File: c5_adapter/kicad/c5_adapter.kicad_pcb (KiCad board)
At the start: 4 copper layers, 50 x 45 mm, 7 parts, among them J1 Conn_01x10, J3 Conn_01x16, J4 Conn_01x16, J5 Conn_01x16, J6 Conn_01x16, SW1 MK-12C02-G020

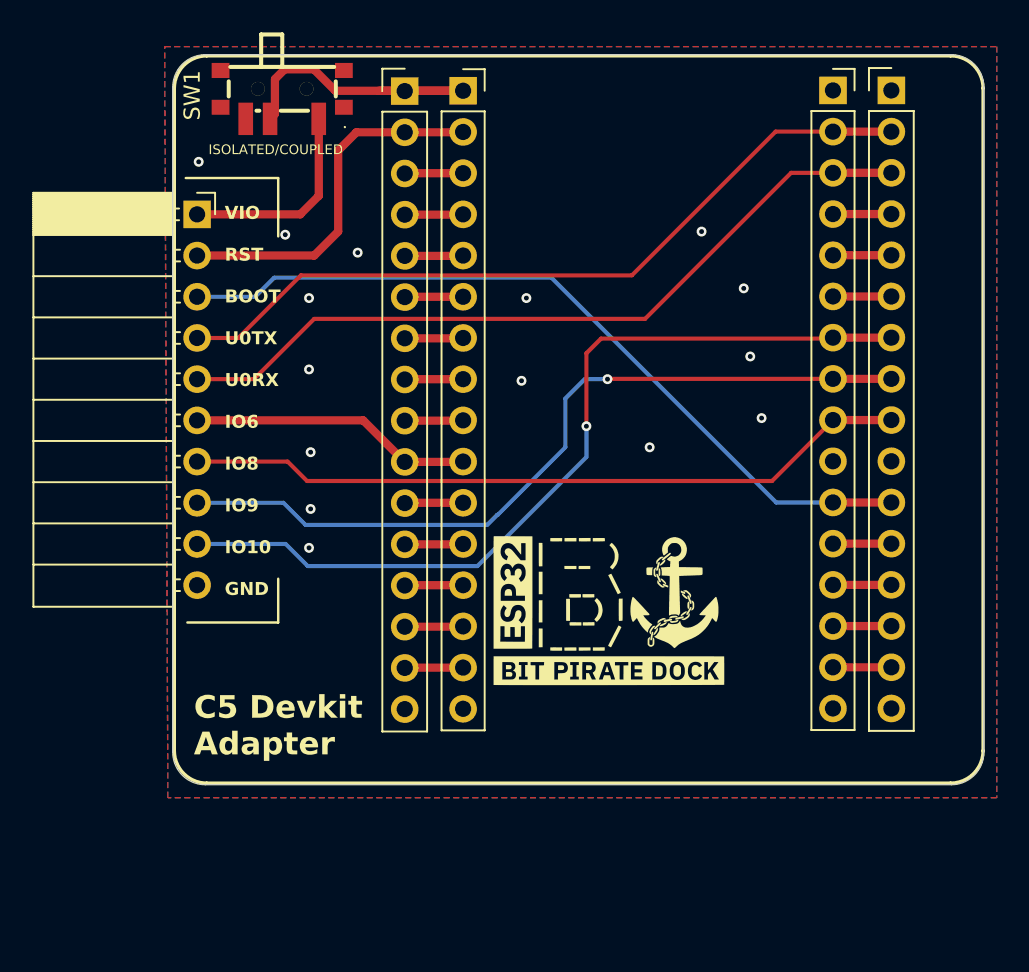
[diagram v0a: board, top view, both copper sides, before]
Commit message: Modified silkscreen markings
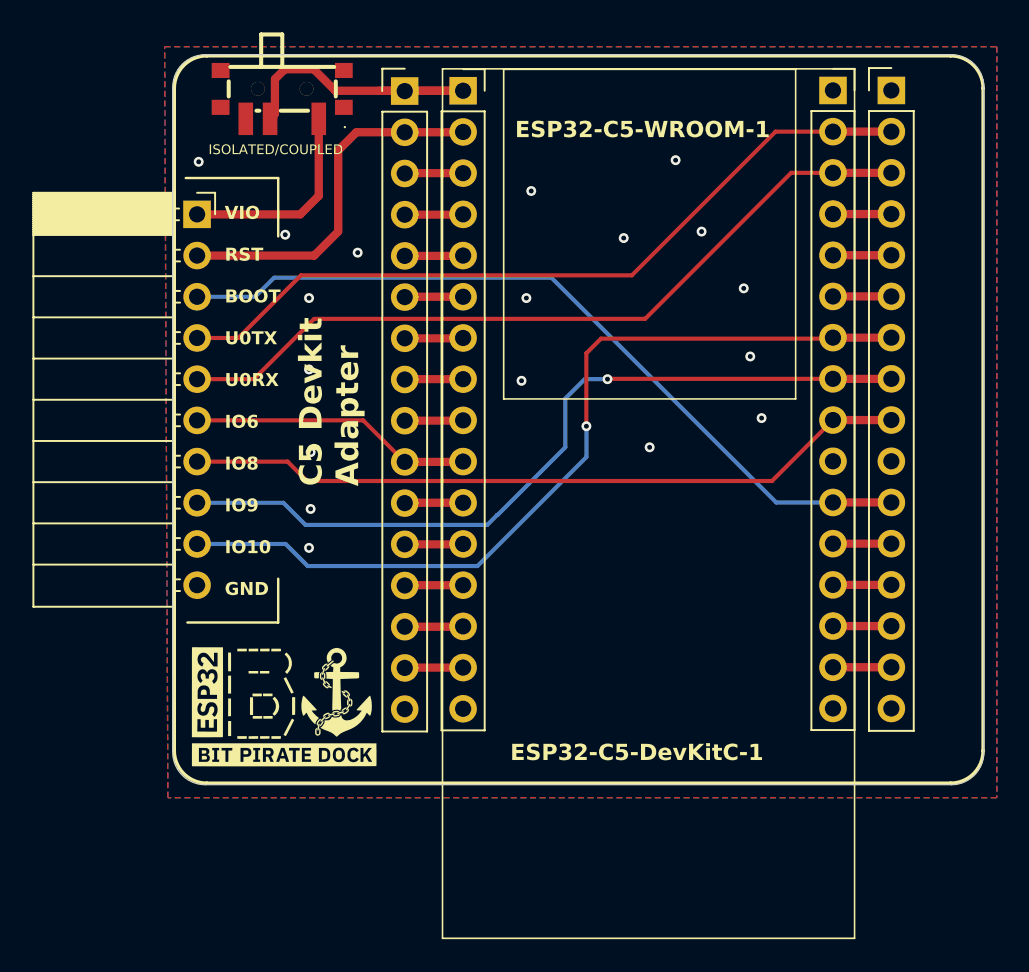
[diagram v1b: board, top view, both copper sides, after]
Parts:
- moved G*** 20.9 mm to (180.0, 118.8)
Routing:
- net GND: vias 15 -> 18
- added copper zone on In1.Cu, net GND
- added copper zone on In2.Cu, net GND
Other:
- board text added: "ESP32-C5-DevKitC-1"
- board text added: "ESP32-C5-WROOM-1"

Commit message: Inverted port writing
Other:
- board text added: "GND IO10 IO9 IO8 IO6 U0RX U0TX BOOT RST VIO"
- board text removed: "VIO RST BOOT U0TX U0RX IO6 IO8 IO9 IO10 GND"
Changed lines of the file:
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@@
 		)
 	)
-	(gr_text "VIO\n\nRST\n\nBOOT\n\nU0TX\n\nU0RX\n\nIO6\n\nIO8\n\nIO9\n\nIO10\n\nGND"
-		(at 176.2 112.3 0)
+	(gr_text "GND\n\nIO10\n\nIO9\n\nIO8\n\nIO6\n\nU0RX\n\nU0TX\n\nBOOT\n\nRST\n\nVIO"
+		(at 179.6 88.1 180)
 		(layer "F.SilkS" knockout)
 		(effects
